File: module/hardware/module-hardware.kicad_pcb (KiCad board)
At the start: 4 copper layers, 45.7 x 125.7 mm, 86 parts, among them J1 USB_B_Micro, J10 Conn_01x03, J11 Conn_01x03, J12 Conn_01x03, J13 0, J2 40Pin 0.1", J3 Conn_01x02_Male, J4 40Pin 0.1", J5 Conn_01x03_Male, J6 Conn_01x03_Male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

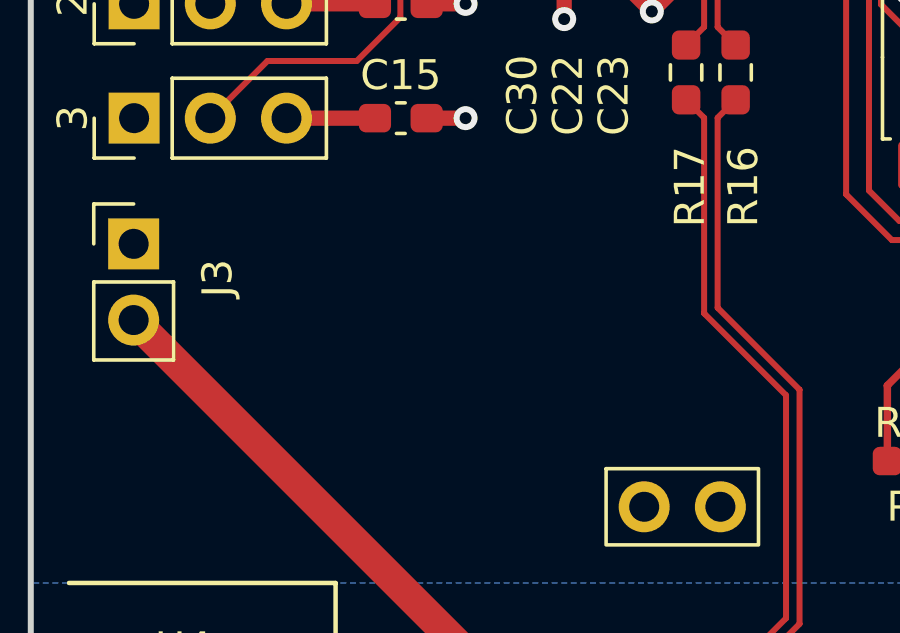
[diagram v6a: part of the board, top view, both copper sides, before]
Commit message: Add DRUM logo
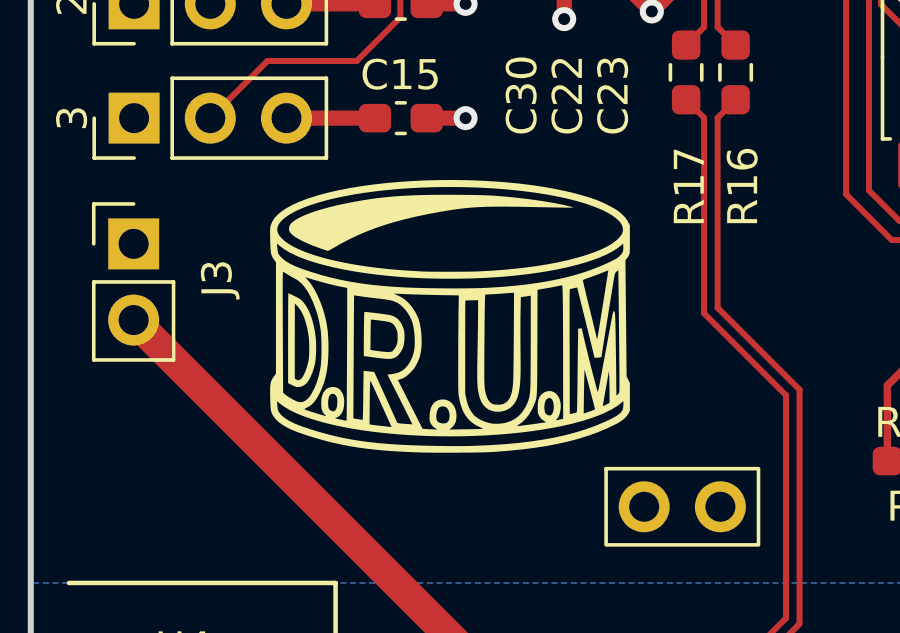
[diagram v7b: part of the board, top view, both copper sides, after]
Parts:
- added G***: LOGO, LOGO, F.Cu at (141.0, 148.6)

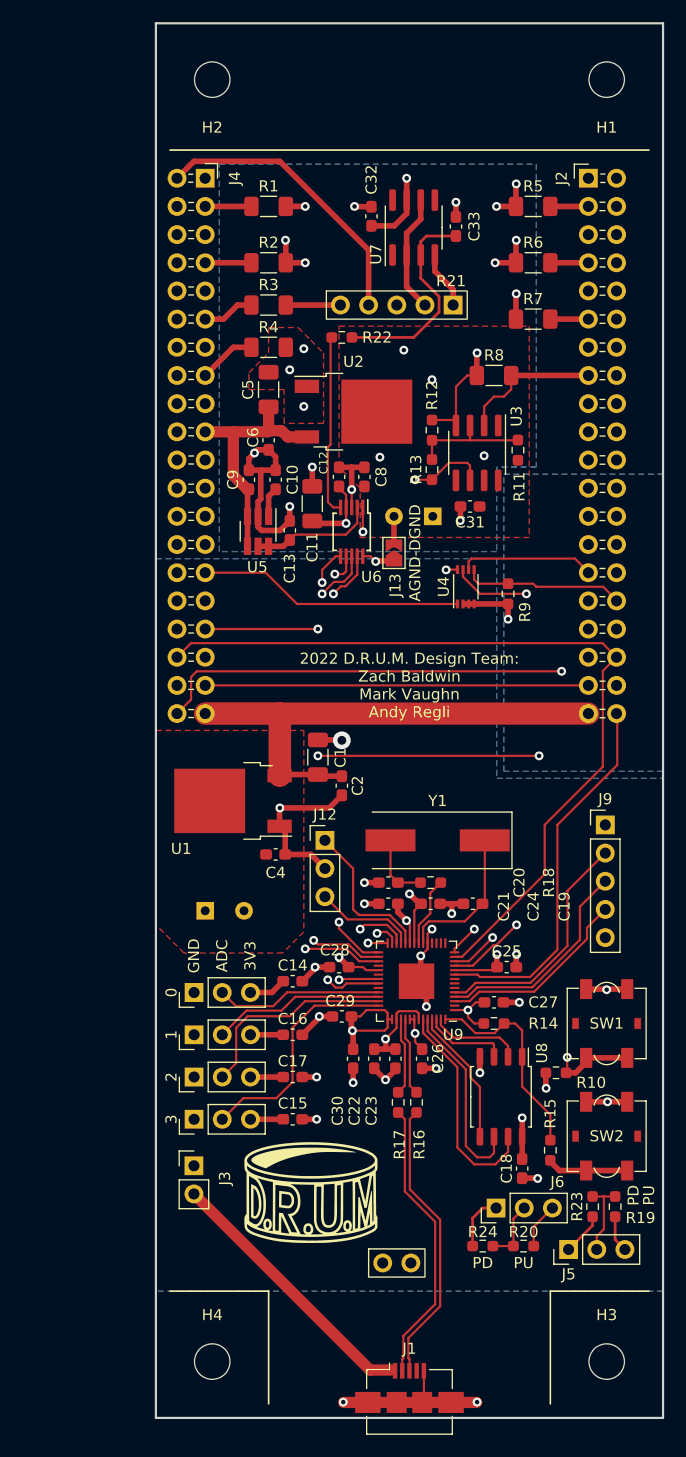
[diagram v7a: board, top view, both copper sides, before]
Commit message: Finalized PCB soldermask labeling for Module
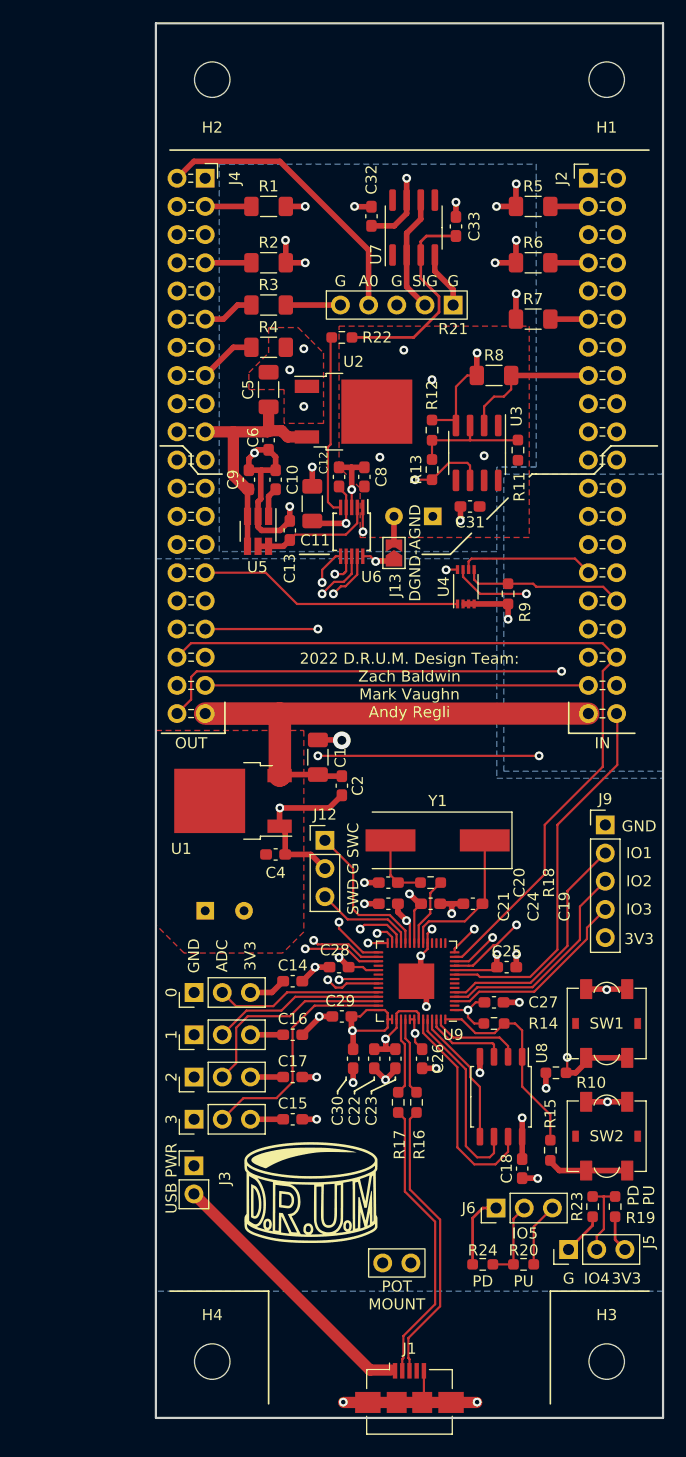
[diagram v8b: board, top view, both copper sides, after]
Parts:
- moved R20 1.65 mm to (160.1, 155.1)
- moved R24 1.65 mm to (156.5, 155.1)
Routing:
- net GND: track 97.0 -> 98.6 mm
- net /D.R.U.M. Module Digital/GPIO5_BTN1: track 43.3 -> 44.9 mm
- net +3V3: track 60.7 -> 62.4 mm
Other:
- board text added: "A0"
- board text added: "DGND-AGND"
- board text added: "G"
- board text added: "IN"
- board text added: "IO1"
- board text added: "IO2"
- board text added: "IO3"
- board text added: "IO4"
- board text added: "IO5"
- board text added: "OUT"
- board text added: "POT MOUNT"
- board text added: "SIG"
- board text added: "SWC"
- board text added: "SWD"
- board text added: "USB PWR"
- board text removed: "AGND-DGND"
